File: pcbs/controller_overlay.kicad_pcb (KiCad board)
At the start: 2 copper layers, 19.7 x 60.1 mm, 2 parts

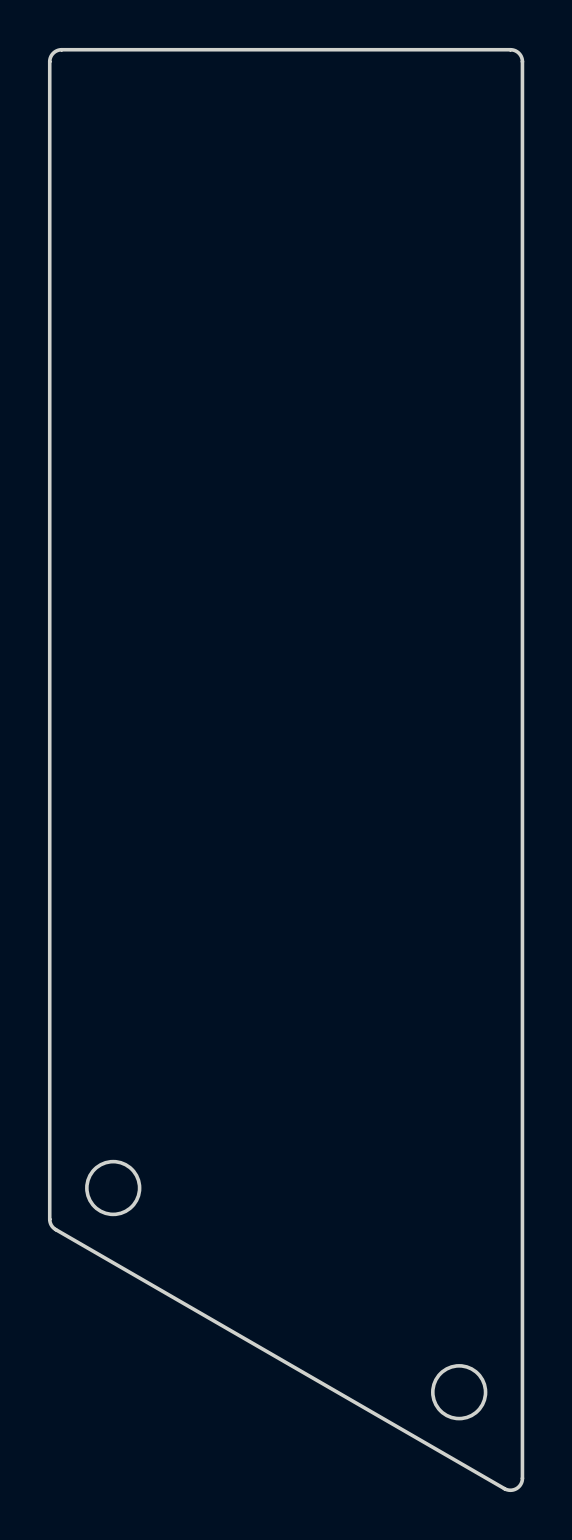
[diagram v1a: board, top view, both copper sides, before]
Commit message: build: generate PCB layouts, routing, gerbers, and preview images
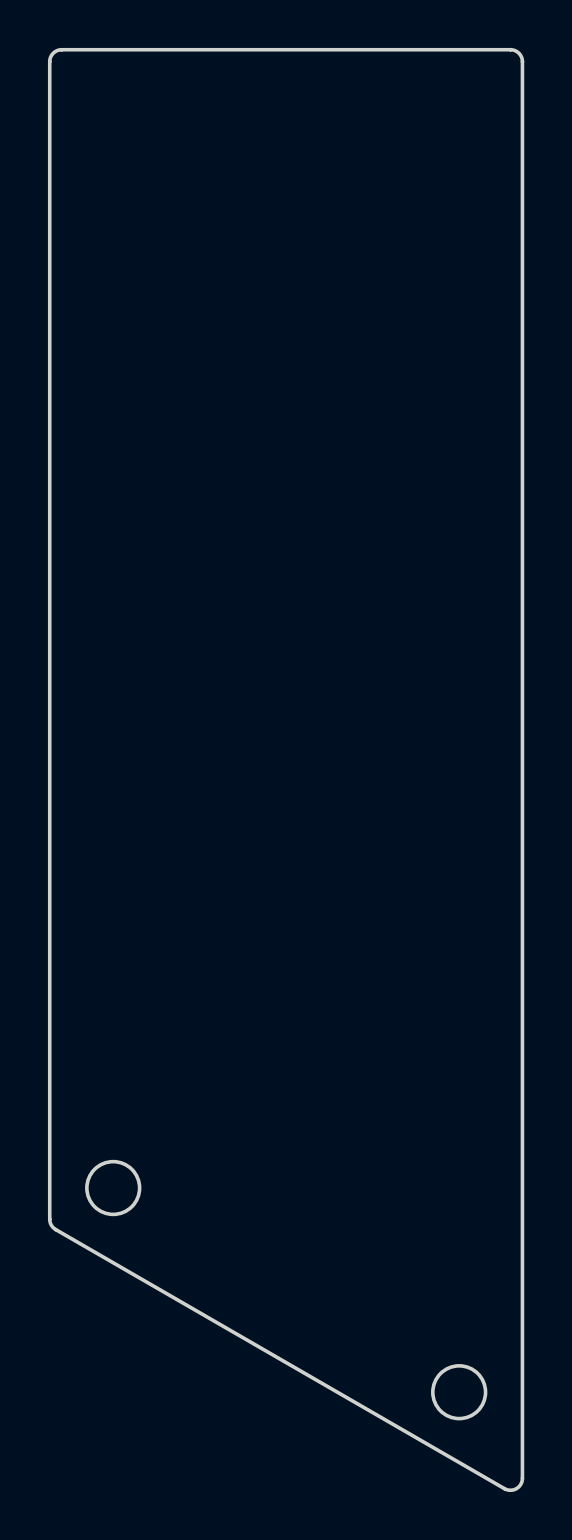
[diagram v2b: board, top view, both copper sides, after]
